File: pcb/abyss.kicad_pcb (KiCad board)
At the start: 2 copper layers, 119.3 x 111.5 mm, 42 parts

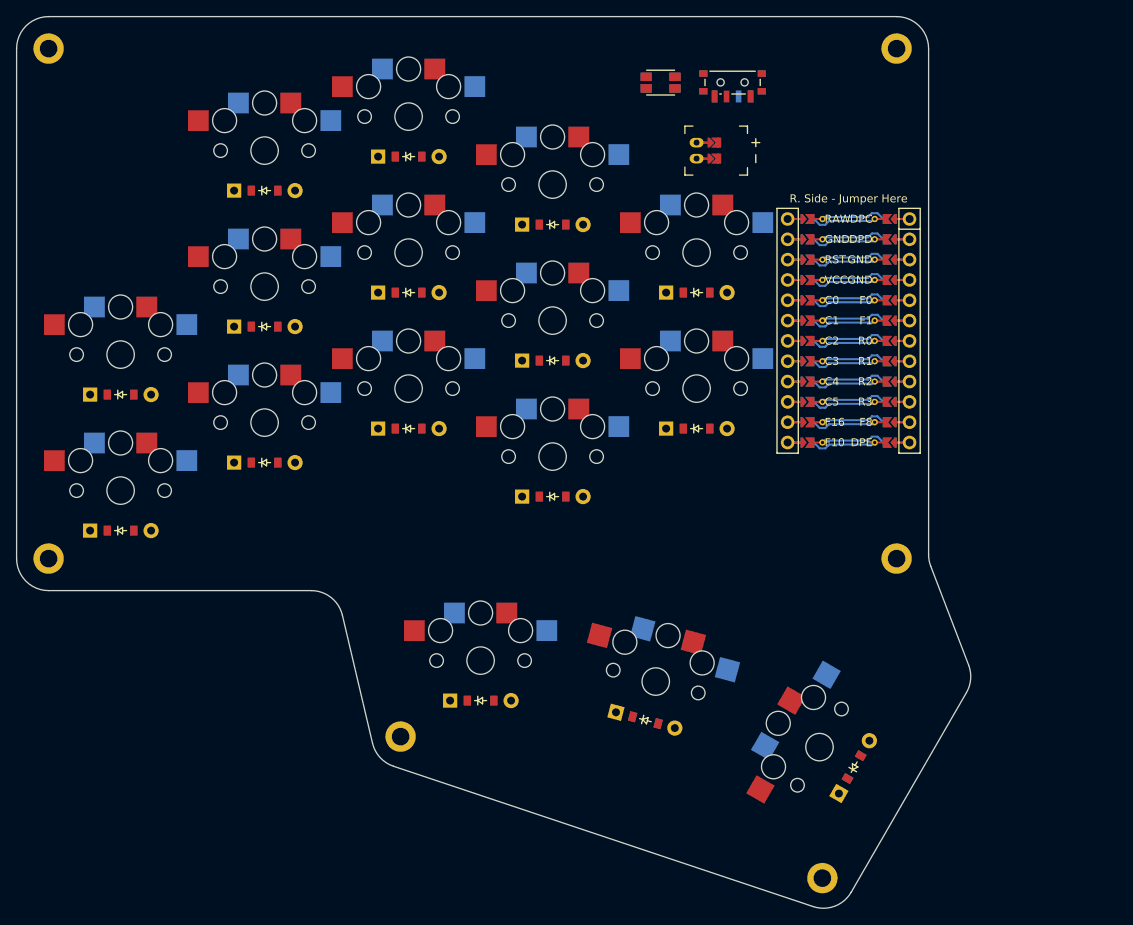
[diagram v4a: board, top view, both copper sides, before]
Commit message: Add mounting holes for the plate on the pcb
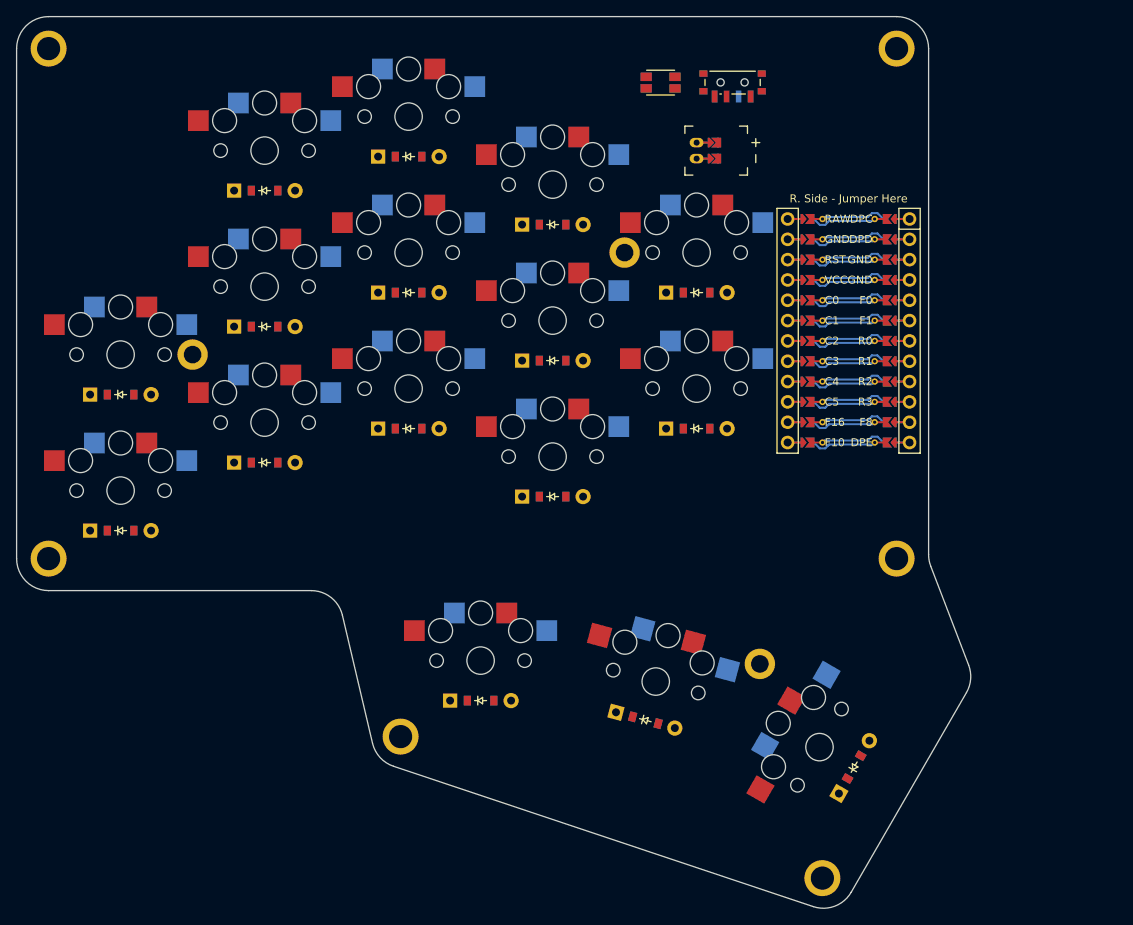
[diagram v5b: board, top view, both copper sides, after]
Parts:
- added H7: , mounting_hole, F.Cu at (109.0, 83.0)
- added H8: , mounting_hole, F.Cu at (163.0, 70.2)
- added H9: , mounting_hole, F.Cu at (179.9, 121.7)
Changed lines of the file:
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@@
+                    (effects (font (size 1 1) (thickness 0.15)))
+                )
+                (pad "" thru_hole circle (at 0 0 180) (size 4.5 4.5) (drill 2.9) (layers *.Cu *.Mask))
+                (fp_circle (center 0 0) (end -2.5 0) (layer F.CrtYd) (width 0.05))
+                (fp_circle (center 0 0) (end -2.5 0) (layer B.CrtYd) (width 0.05))
+            )
+            (module mounting_hole (layer F.Cu)
+                (at 197 44.75 0)
+                (fp_text reference "H2" (at 0 3) (layer F.SilkS) hide
+                    (effects (font (size 1 1) (thickness 0.15)))
+                )
+                (pad "" thru_hole circle (at 0 0 180) (size 4.5 4.5) (drill 2.9) (layers *.Cu *.Mask))
+                (fp_circle (center 0 0) (end -2.5 0) (layer F.CrtYd) (width 0.05))
+                (fp_circle (center 0 0) (end -2.5 0) (layer B.CrtYd) (width 0.05))
+            )
+            (module mounting_hole (layer F.Cu)
+                (at 197 108.5 0)
+                (fp_text reference "H3" (at 0 3) (layer F.SilkS) hide
+                    (effects (font (size 1 1) (thickness 0.15)))
+                )
+                (pad "" thru_hole circle (at 0 0 180) (size 4.5 4.5) (drill 2.9) (layers *.Cu *.Mask))
+                (fp_circle (center 0 0) (end -2.5 0) (layer F.CrtYd) (width 0.05))
+                (fp_circle (center 0 0) (end -2.5 0) (layer B.CrtYd) (width 0.05))
+            )
+            (module mounting_hole (layer F.Cu)
+                (at 91 108.5 0)
+                (fp_text reference "H4" (at 0 3) (layer F.SilkS) hide
+                    (effects (font (size 1 1) (thickness 0.15)))
+                )
+                (pad "" thru_hole circle (at 0 0 180) (size 4.5 4.5) (drill 2.9) (layers *.Cu *.Mask))
+                (fp_circle (center 0 0) (end -2.5 0) (layer F.CrtYd) (width 0.05))
+                (fp_circle (center 0 0) (end -2.5 0) (layer B.CrtYd) (width 0.05))
+            )
+            (module mounting_hole (layer F.Cu)
+                (at 135 130.75 0)
+                (fp_text reference "H5" (at 0 3) (layer F.SilkS) hide
+                    (effects (font (size 1 1) (thickness 0.15)))
+                )
+                (pad "" thru_hole circle (at 0 0 180) (size 4.5 4.5) (drill 2.9) (layers *.Cu *.Mask))
+                (fp_circle (center 0 0) (end -2.5 0) (layer F.CrtYd) (width 0.05))
+                (fp_circle (center 0 0) (end -2.5 0) (layer B.CrtYd) (width 0.05))
+            )
+            (module mounting_hole (layer F.Cu)
+                (at 187.72396099999997 148.4395207 60)
+                (fp_text reference "H6" (at 0 3) (layer F.SilkS) hide
+                    (effects (font (size 1 1) (thickness 0.15)))
+                )
+                (pad "" thru_hole circle (at 0 0 180) (size 4.5 4.5) (drill 2.9) (layers *.Cu *.Mask))
+                (fp_circle (center 0 0) (end -2.5 0) (layer F.CrtYd) (width 0.05))
+                (fp_circle (center 0 0) (end -2.5 0) (layer B.CrtYd) (width 0.05))
+            )
+            (module mounting_hole (layer F.Cu)
+                (at 109 83 0)
+                (fp_text reference "H7" (at 0 3) (layer F.SilkS) hide
                     (effects (font (size 1 1) (thickness 0.15)))
                 )
@@
             )
             (module mounting_hole (layer F.Cu)
-                (at 197 44.75 0)
-                (fp_text reference "H2" (at 0 3) (layer F.SilkS) hide
+                (at 163 70.25 0)
+                (fp_text reference "H8" (at 0 3) (layer F.SilkS) hide
                     (effects (font (size 1 1) (thickness 0.15)))
                 )
@@
             )
             (module mounting_hole (layer F.Cu)
-                (at 197 108.5 0)
-                (fp_text reference "H3" (at 0 3) (layer F.SilkS) hide
+                (at 179.90790900000002 121.6622384 -15)
+                (fp_text reference "H9" (at 0 3) (layer F.SilkS) hide
                     (effects (font (size 1 1) (thickness 0.15)))
                 )
-                (pad "" thru_hole circle (at 0 0 180) (size 3.8000000000000003 3.8000000000000003) (drill 2.2) (layers *.Cu *.Mask))
-                (fp_circle (center 0 0) (end -2.1500000000000004 0) (layer F.CrtYd) (width 0.05))
-                (fp_circle (center 0 0) (end -2.1500000000000004 0) (layer B.CrtYd) (width 0.05))
-            )
-            (module mounting_hole (layer F.Cu)
-                (at 91 108.5 0)
-                (fp_text reference "H4" (at 0 3) (layer F.SilkS) hide
-                    (effects (font (size 1 1) (thickness 0.15)))
-                )
-                (pad "" thru_hole circle (at 0 0 180) (size 3.8000000000000003 3.8000000000000003) (drill 2.2) (layers *.Cu *.Mask))
-                (fp_circle (center 0 0) (end -2.1500000000000004 0) (layer F.CrtYd) (width 0.05))
-                (fp_circle (center 0 0) (end -2.1500000000000004 0) (layer B.CrtYd) (width 0.05))
-            )
-            (module mounting_hole (layer F.Cu)
-                (at 135 130.75 0)
-                (fp_text reference "H5" (at 0 3) (layer F.SilkS) hide
-                    (effects (font (size 1 1) (thickness 0.15)))
-                )
-                (pad "" thru_hole circle (at 0 0 180) (size 3.8000000000000003 3.8000000000000003) (drill 2.2) (layers *.Cu *.Mask))
-                (fp_circle (center 0 0) (end -2.1500000000000004 0) (layer F.CrtYd) (width 0.05))
-                (fp_circle (center 0 0) (end -2.1500000000000004 0) (layer B.CrtYd) (width 0.05))
-            )
-            (module mounting_hole (layer F.Cu)
-                (at 187.72396099999997 148.4395207 60)
-                (fp_text reference "H6" (at 0 3) (layer F.SilkS) hide
-                    (effects (font (size 1 1) (thickness 0.15)))
-                )

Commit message: Route pcb
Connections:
- MCU1 pad 120: F0 -> (no net)
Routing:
- net C1: track 0.00 -> 200.8 mm, vias 0 -> 4
- net C3: track 0.00 -> 185.5 mm, vias 0 -> 4
- net C4: track 0.00 -> 142.7 mm, vias 0 -> 3
- net R0: track 0.00 -> 129.3 mm
- net R3: track 0.00 -> 129.0 mm
- net R1: track 50.9 -> 179.5 mm, vias 0 -> 1
- net R2: track 50.9 -> 161.1 mm
- net index_bottom: track 122.0 -> 34.2 mm
- net GND: track 0.00 -> 74.4 mm
- net C2: track 0.00 -> 73.9 mm, vias 0 -> 3
- net C0: track 122.1 -> 189.4 mm, vias 0 -> 3
- net RST: track 0.00 -> 66.0 mm
- net C5: track 0.00 -> 62.4 mm, vias 0 -> 1
- net pinky_home: track 0.00 -> 36.8 mm
- net left_cluster: track 0.00 -> 34.2 mm
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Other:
- net class Default removed

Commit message: Finish pcb routing
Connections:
- MCU1 pad 120: (no net) -> F0
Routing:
- net C2: track 73.9 -> 187.6 mm, vias 3 -> 4
- net RAW: track 16.3 -> 44.5 mm, vias 0 -> 2
- net GND: track 74.4 -> 98.0 mm, vias 0 -> 2
- net R3: track 129.0 -> 138.4 mm, vias 0 -> 1
- net C4: track 142.7 -> 139.5 mm
- net C3: track 185.5 -> 182.6 mm
- net RST: track 66.0 -> 68.5 mm, vias 0 -> 1
- net C5: track 62.4 -> 64.5 mm
- net C1: track 200.8 -> 202.9 mm
- net R2: track 161.1 -> 162.1 mm
- net BAT_P: vias 0 -> 1
